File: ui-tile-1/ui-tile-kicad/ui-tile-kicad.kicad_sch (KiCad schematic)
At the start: 26 parts, among them SW1 SKRPABE010, SW2 SKRPABE010, U1 RP2040, U2 W25Q16JVUXIQ, X1 12MHz

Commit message: continuing with ui-tile
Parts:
- R2, R3: value 27.4 -> 27.4R
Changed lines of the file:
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@@
 			)
 		)
-		(property "Value" "27.4"
+		(property "Value" "27.4R"
 			(at 121.666 76.962 0)
 			(show_name no)
@@
 			)
 		)
-		(property "Value" "27.4"
+		(property "Value" "27.4R"
 			(at 121.666 70.612 0)
 			(show_name no)

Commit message: removed warnings from schematic
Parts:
- removed C1, C2: 22pF, jlcpcb:C0402, symbol jlcpcb:0402CG220J500NT
- added C11, C12: 30pF, jlcpcb:C0402, symbol jlcpcb:0402CG300J500NT
- added C13, C17: 100nF, jlcpcb:C0402, symbol jlcpcb:CL05B104KO5NNNC
- added C14, C16: 10uF, jlcpcb:C0805, symbol jlcpcb:CL21A106KOQNNNE
- added LED1, LED2: KT-0603R, jlcpcb:LED-SMD_L1.6-W0.8-R-RD, symbol jlcpcb:KT-0603R
- added R8: 1k, jlcpcb:R0402, symbol jlcpcb:0402WGF1001TCE
- added R9: 1.5k, jlcpcb:R0603, symbol jlcpcb:0603WAF1501T5E
- added U3: NCP1117ST33T3G, jlcpcb:SOT-223-3_L6.5-W3.4-P2.30-LS7.0-BR, symbol jlcpcb:NCP1117ST33T3G
- renumbered C11 to C1, C20 to C10, C21 to C15, C13 to C2, C12 to C3, C14 to C4, C15 to C5, C16 to C6, C17 to C7, C18 to C8, C19 to C9, R2 to R1, R3 to R2, R7 to R3, R6 to R4, R1 to R5, R5 to R6, R4 to R7, SW2 to SW1, SW1 to SW2
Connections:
- net QSP_SCLK is gone; now on net QSPI_SCLK: U2.6 (CLK)
- net +3V3: now also U1.44 (VREG_IN), C16.2, C17.2, R8.1, U3.2 (OUTPUT), U3.4 (TAB)
- net GND: now also C11.1, C12.1, C13.1, C14.1, C16.1, C17.1, LED1.2 (K), LED2.2 (K), U3.1 (ADJ/GND)
- net USB_D+: now also R1.1; no longer R1.2
- net USB_D-: now also R2.1; no longer R2.2
- net USB_VSYS: now also C13.2, C14.2, R9.1, U3.3 (INPUT)
- net XIN: now also C11.2
- net at R5.1, X1.3 (OSC2): now also C12.2
- net at U1.46 (USB_DM): now also R2.2; no longer R2.1
- net at U1.47 (USB_DP): now also R1.2; no longer R1.1
- net QSPI_CLK renamed QSPI_SCLK
- new net: LED1.1 (A), R8.2
- new net: LED2.1 (A), R9.2
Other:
- note added: "Give some copper pour/vias for TAB heatsink"
- note added: "Power LED's"
- note added: "USB Connector"
- note added: "Voltage Regulator 5V -> 3.3V"
- moved on the sheet: R1, R2

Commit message: finished first pass at rp2040 basics
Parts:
- added D1, D2: B5819W_C8598, jlcpcb:SOD-123_L2.7-W1.6-LS3.7-RD-1, symbol jlcpcb:B5819W_C8598
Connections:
- net USB_VSYS renamed VSYS
- net VSYS: now also D1.1 (-), D2.1 (-); no longer USBC1.A4-B9 (VBUS), USBC1.B4-A9 (VBUS)
- new net +5V: D2.2 (+)
- new net USB_VBUS: D1.2 (+), USBC1.A4-B9 (VBUS), USBC1.B4-A9 (VBUS)
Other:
- note added: "Power OR (from USB or onboard +5V)"
- note added: "Route these as matched differential pair"
- moved on the sheet: C13, C14, C16, C17, LED1, LED2, R8, R9, U3

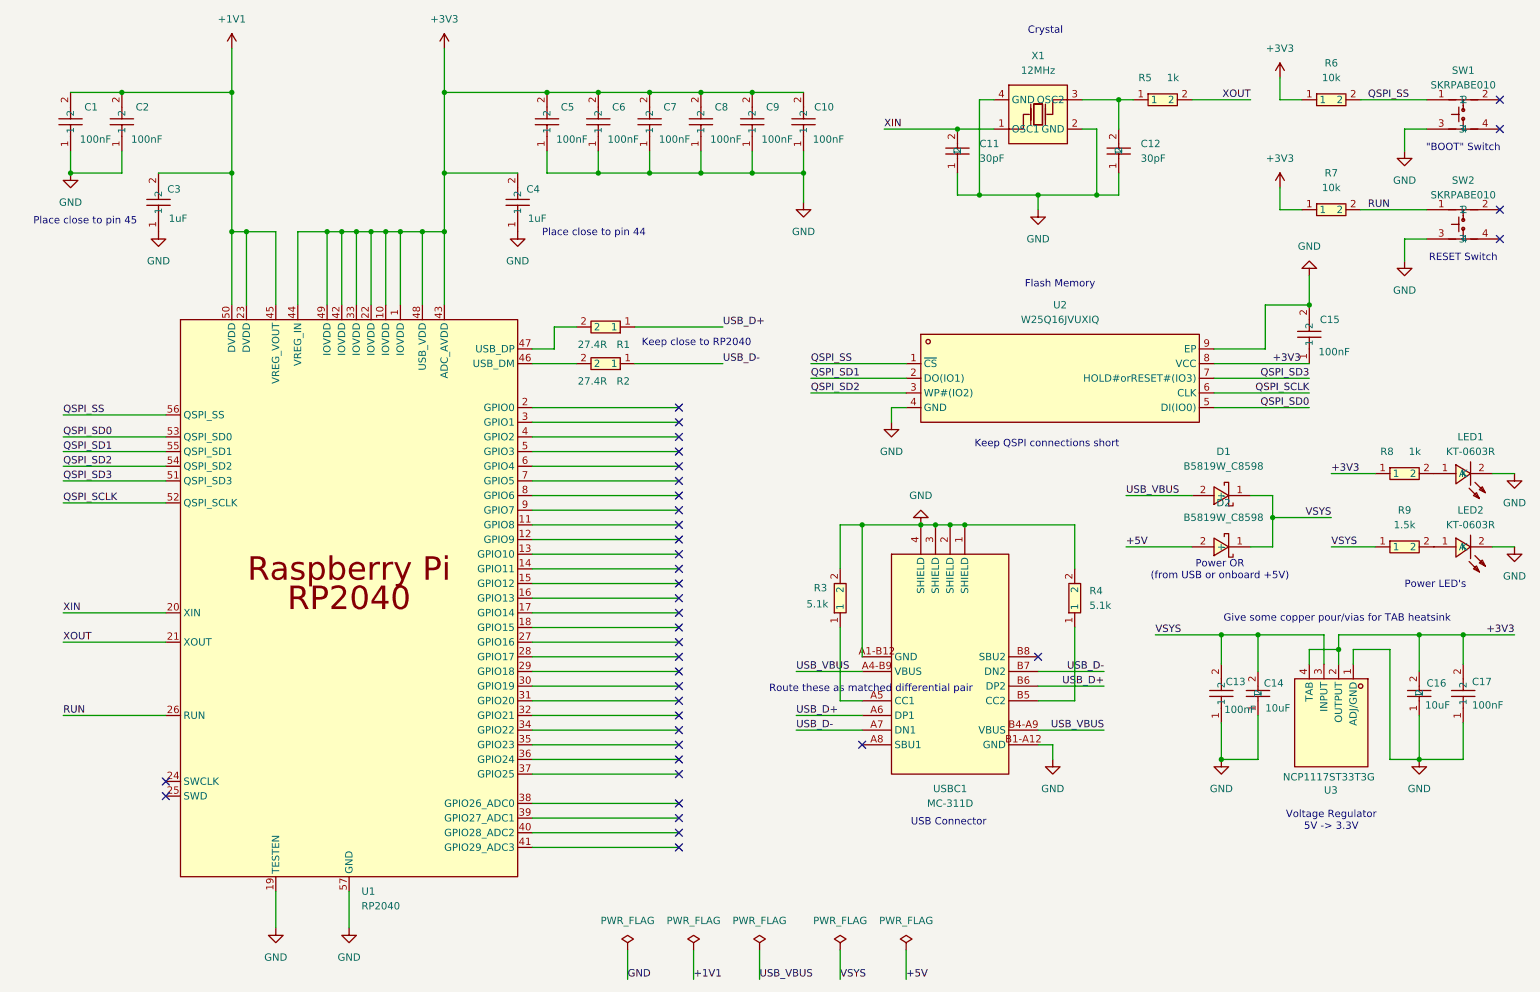
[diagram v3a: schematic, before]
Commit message: started breaking out into sub sheets
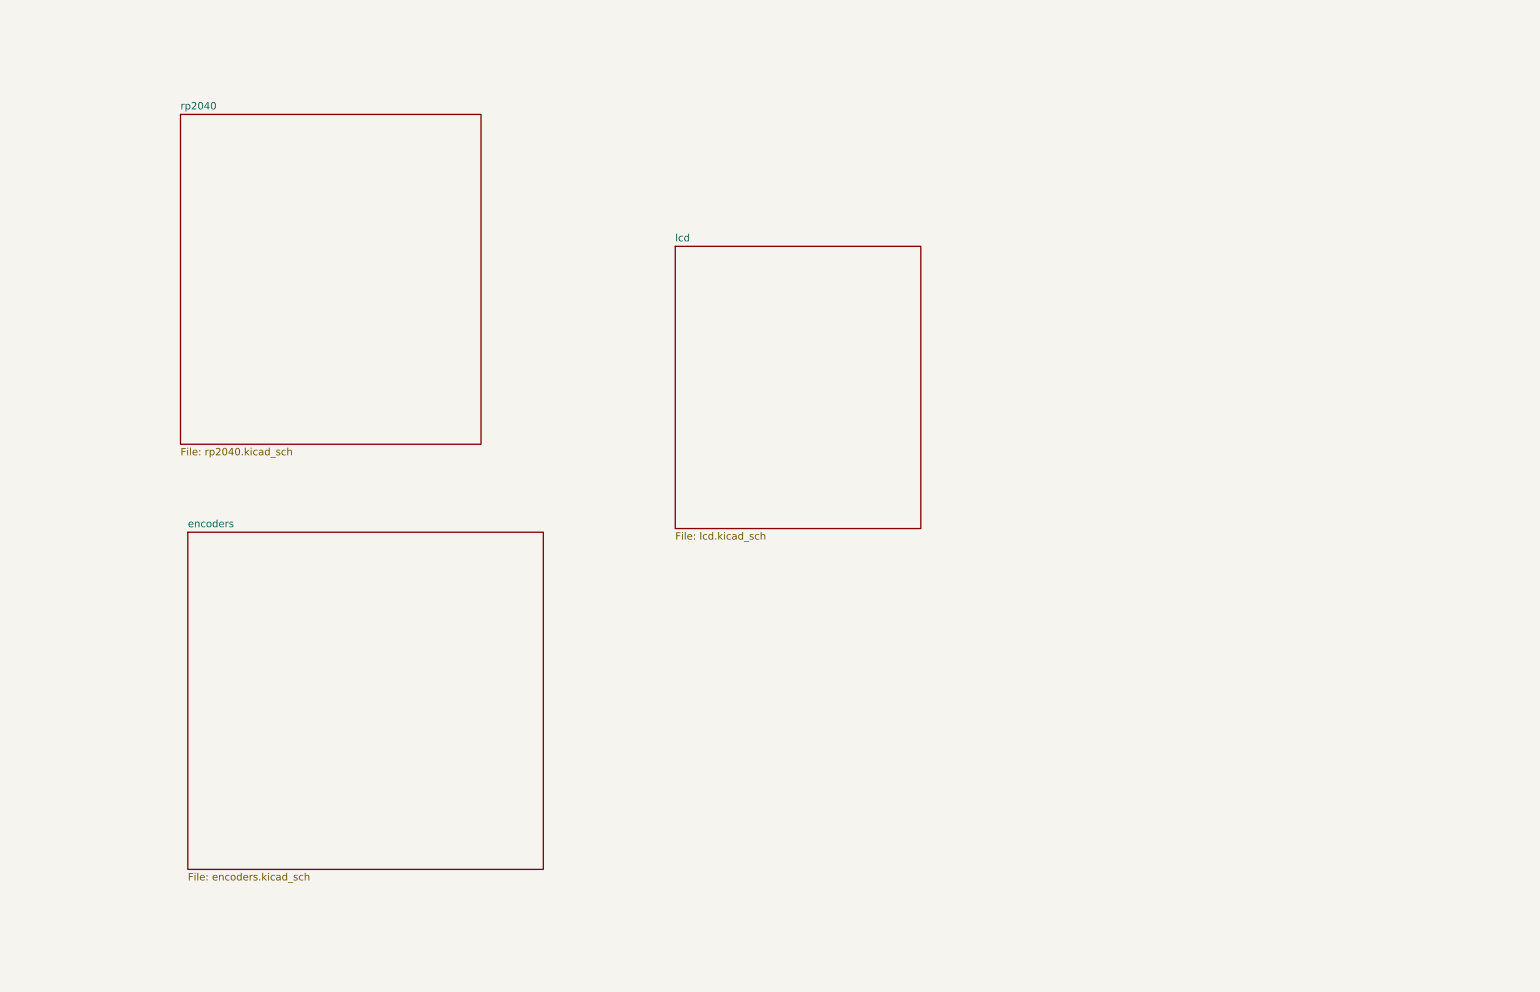
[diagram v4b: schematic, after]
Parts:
- removed C1, C10, C13, C15, C17, C2, C5, C6, C7, C8, C9: 100nF, jlcpcb:C0402, symbol jlcpcb:CL05B104KO5NNNC
- removed C11, C12: 30pF, jlcpcb:C0402, symbol jlcpcb:0402CG300J500NT
- removed C14, C16: 10uF, jlcpcb:C0805, symbol jlcpcb:CL21A106KOQNNNE
- removed C3, C4: 1uF, jlcpcb:C0402, symbol jlcpcb:CL05A105KA5NQNC
- removed D1, D2: B5819W_C8598, jlcpcb:SOD-123_L2.7-W1.6-LS3.7-RD-1, symbol jlcpcb:B5819W_C8598
- removed LED1, LED2: KT-0603R, jlcpcb:LED-SMD_L1.6-W0.8-R-RD, symbol jlcpcb:KT-0603R
- removed R1, R2: 27.4R, jlcpcb:R0402, symbol jlcpcb:0402WGF274JTCE
- removed R3, R4: 5.1k, jlcpcb:R0402, symbol jlcpcb:0402WGF5101TCE
- removed R5, R8: 1k, jlcpcb:R0402, symbol jlcpcb:0402WGF1001TCE
- removed R6, R7: 10k, jlcpcb:R0402, symbol jlcpcb:0402WGF1002TCE
- removed R9: 1.5k, jlcpcb:R0603, symbol jlcpcb:0603WAF1501T5E
- removed SW1, SW2: SKRPABE010, jlcpcb:KEY-SMD_4P-L4.2-W3.2-P2.20-LS4.6, symbol jlcpcb:SKRPABE010
- removed U1: RP2040, jlcpcb:LQFN-56_L7.0-W7.0-P0.4-EP, symbol jlcpcb:RP2040
- removed U2: W25Q16JVUXIQ, jlcpcb:USON-8_L3.0-W2.0-P0.50-BL-EP, symbol jlcpcb:W25Q16JVUXIQ
- removed U3: NCP1117ST33T3G, jlcpcb:SOT-223-3_L6.5-W3.4-P2.30-LS7.0-BR, symbol jlcpcb:NCP1117ST33T3G
- removed USBC1: MC-311D, jlcpcb:USB-C-SMD_MC-311D, symbol jlcpcb:MC-311D
- removed X1: 12MHz, jlcpcb:CRYSTAL-SMD_4P-L3.2-W2.5-BL, symbol jlcpcb:X322512MSB4SI
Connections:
- no-connect marks 38 -> 0
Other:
- added sheet encoders (encoders.kicad_sch)
- added sheet lcd (lcd.kicad_sch)
- added sheet rp2040 (rp2040.kicad_sch)
- note removed: ""BOOT" Switch"
- note removed: "Crystal"
- note removed: "Flash Memory"
- note removed: "Give some copper pour/vias for TAB heatsink"
- note removed: "Keep QSPI connections short"
- note removed: "Keep close to RP2040"
- note removed: "Place close to pin 44"
- note removed: "Place close to pin 45"
- note removed: "Power LED's"
- note removed: "Power OR (from USB or onboard +5V)"
- note removed: "RESET Switch"
- note removed: "Route these as matched differential pair"
- note removed: "USB Connector"
- note removed: "Voltage Regulator 5V -> 3.3V"

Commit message: finished schematic electricals
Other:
- added sheet headers (headers.kicad_sch)
- added sheet leds (leds.kicad_sch)
- sheet encoders ports: added Enc1_A, Enc1_B, Enc1_SW, Enc2_A, Enc2_B, Enc2_SW, Enc3_A, Enc3_B, Enc3_SW, Enc4_A, Enc4_B, Enc4_SW; removed none
- sheet lcd ports: added BL, CS, DC, MOSI, RES, SCK; removed none
- sheet rp2040 ports: added Enc1_A, Enc1_B, Enc1_SW, Enc2_A, Enc2_B, Enc2_SW, Enc3_A, Enc3_B, Enc3_SW, Enc4_A, Enc4_B, Enc4_SW, LCD_BL, LCD_CS, LCD_DC, LCD_MOSI, LCD_RST, LCD_SCK, LED_OUT, MB_CS, MB_IRQ, MB_MISO, MB_MOSI, MB_SCK; removed none

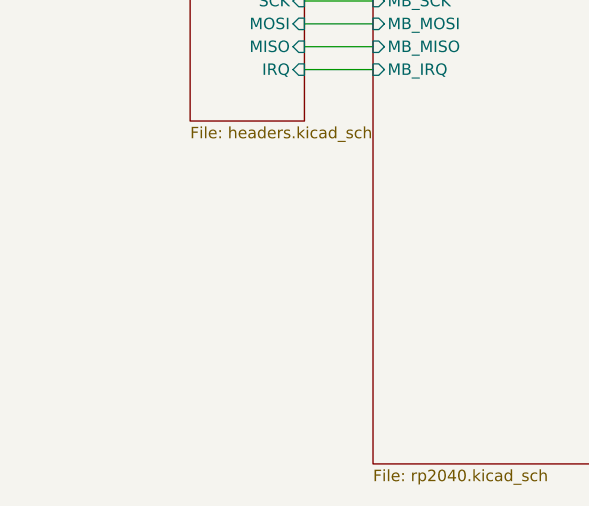
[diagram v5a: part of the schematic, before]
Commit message: Added mounting holes
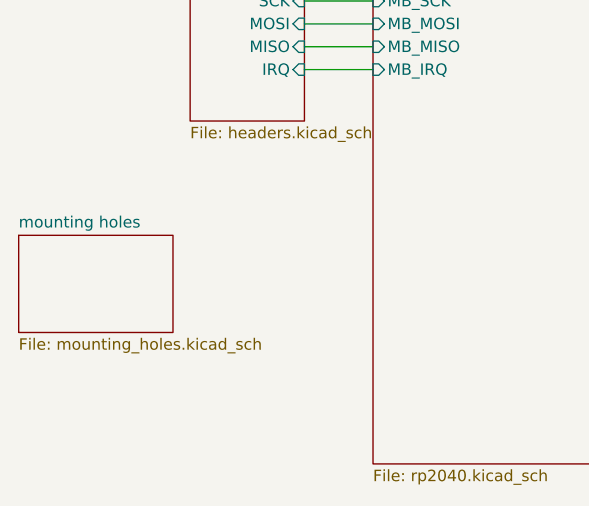
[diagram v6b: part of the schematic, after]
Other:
- added sheet mounting holes (mounting_holes.kicad_sch)
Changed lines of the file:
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@@
+	)
+	(sheet
+		(at 33.02 90.805)
+		(size 17.145 10.795)
+		(exclude_from_sim no)
+		(in_bom yes)
+		(on_board yes)
+		(dnp no)
+		(fields_autoplaced yes)
+		(stroke
+			(width 0.1524)
+			(type solid)
+		)
+		(fill
+			(color 0 0 0 0)
+		)
+		(property "Sheetname" "mounting holes"
+			(at 33.02 90.0934 0)
+			(show_name no)
+			(do_not_autoplace no)
+			(effects
+				(font
+					(size 1.27 1.27)
+				)
+				(justify left bottom)
+			)
+		)
+		(property "Sheetfile" "mounting_holes.kicad_sch"
+			(at 33.02 102.1846 0)
+			(show_name no)
+			(do_not_autoplace no)
+			(effects
+				(font
+					(size 1.27 1.27)
+				)
+				(justify left top)
+			)
+		)
+		(instances
+			(project "ui-tile-kicad"
+				(path "/217f9734-29d5-465f-84f0-e59e73a19da8"
+					(page "7")
+				)
+			)
+		)
 	)
 	(sheet
